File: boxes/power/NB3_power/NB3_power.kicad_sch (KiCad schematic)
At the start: 31 parts, among them J1 Barrel_Jack_PJ-036AH-SMT-TR, J2 Conn_01x04_Male, SW1 SW_SPDT, U1 Voltage_Regulator_AP64501

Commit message: Final draft (rev 0.0.1) of NB3_power PCB
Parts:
- added D2: LED, LED_SMD:LED_0603_1608Metric, symbol Device:LED
- added R6: 1.6k, Resistor_SMD:R_0402_1005Metric, symbol Device:R
- J2: footprint Connector_PinHeader_2.54mm:PinHeader_1x04_P2.54mm_Vertical_SMD_Pin1Right -> NB3_power:PinHeader_TSM-104-01-L-SH
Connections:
- net +5V: now also J2.1 (Pin_1), J2.2 (Pin_2), D2.2 (A); no longer J2.3 (Pin_3), J2.4 (Pin_4)
- net GND: now also J2.3 (Pin_3), J2.4 (Pin_4), R6.2; no longer J2.1 (Pin_1), J2.2 (Pin_2)
- new net: D2.1 (K), R6.1
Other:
- moved on the sheet: J2

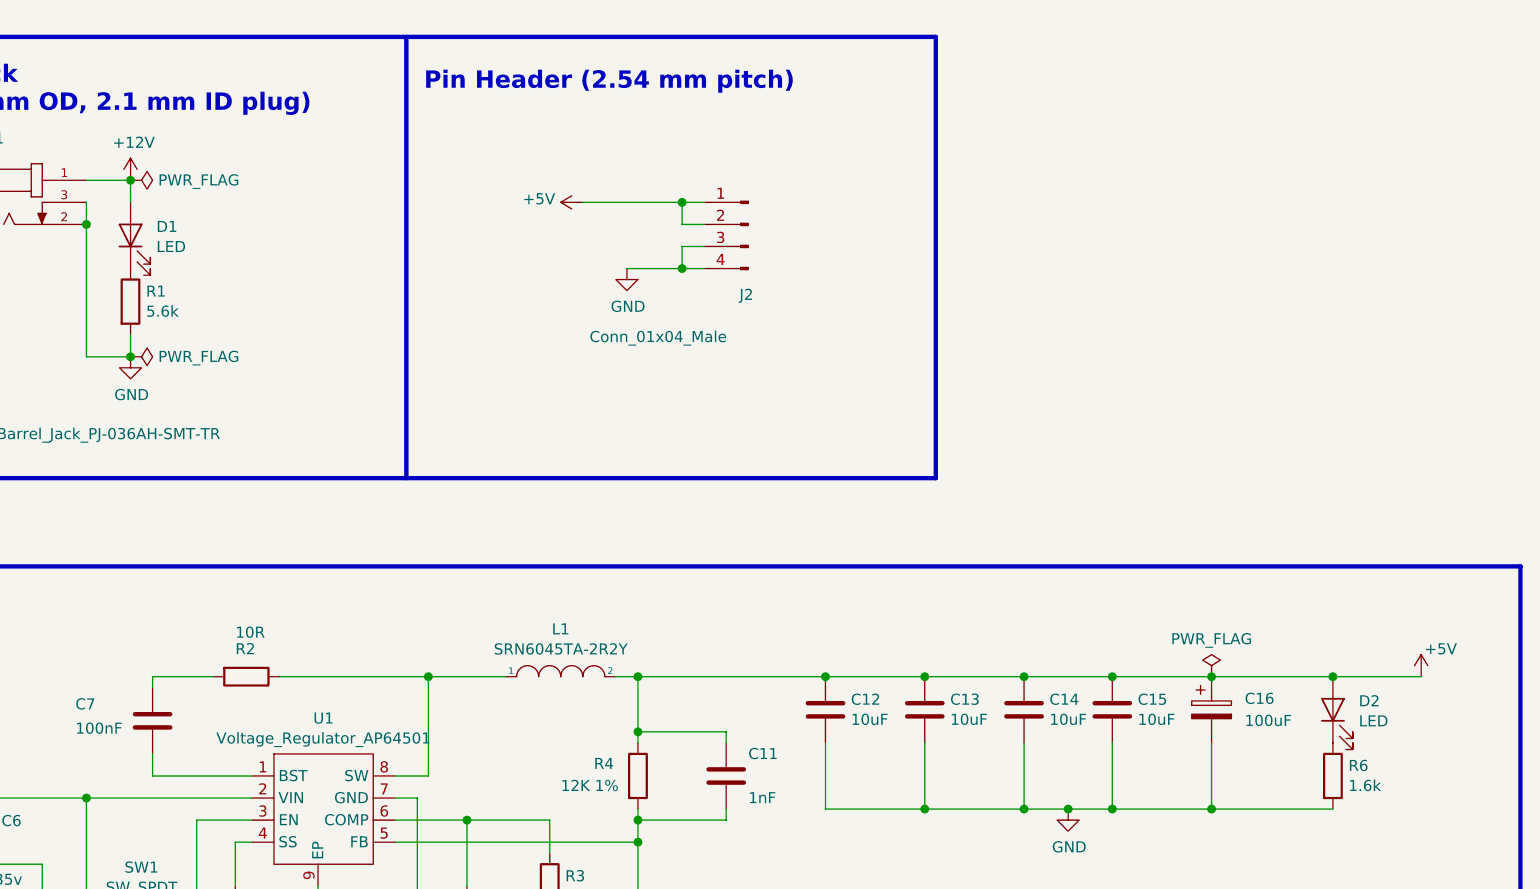
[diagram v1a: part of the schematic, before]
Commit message: Optimized NB3_power BOM for cost
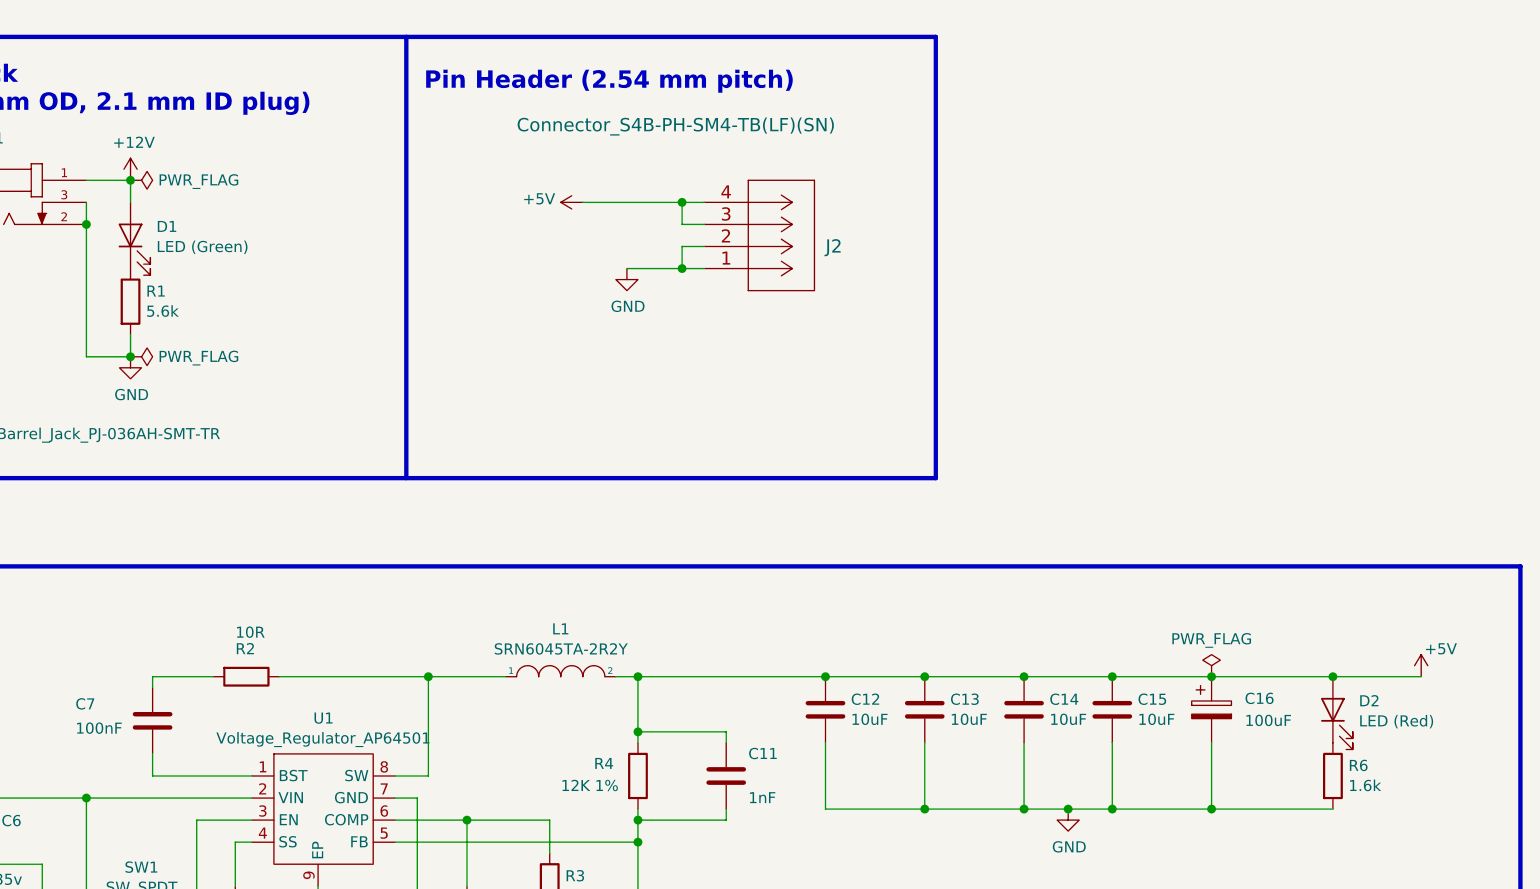
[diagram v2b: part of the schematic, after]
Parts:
- removed J2: Conn_01x04_Male, NB3_power:PinHeader_TSM-104-01-L-SH, symbol Connector:Conn_01x04_Male
- added J2: Connector_S4B-PH-SM4-TB(LF)(SN), NB3_power:Connector_S4B-PH-SM4-TB(LF)(SN), symbol NB3_power:Connector_S4B-PH-SM4-TB(LF)(SN)
- D1: value LED -> LED (Green)
- D2: value LED -> LED (Red)
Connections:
- net +5V: now also J2.3, J2.4
- net GND: now also J2.1, J2.2
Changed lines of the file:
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@@
       (effects (font (size 1.27 1.27)) (justify right))
     )
-    (property "Value" "LED" (id 1) (at 126.1618 54.6608 90)
+    (property "Value" "LED (Green)" (id 1) (at 126.1618 54.6608 90)
       (effects (font (size 1.27 1.27)) (justify right))
     )
@@
       (effects (font (size 1.27 1.27)) (justify right))
     )
-    (property "Value" "LED" (id 1) (at 264.5918 109.2708 90)
+    (property "Value" "LED (Red)" (id 1) (at 264.5918 109.2708 90)
       (effects (font (size 1.27 1.27)) (justify right))
     )
@@
     (pin "1")
     (pin "2")
-  )
-  (symbol (lib_id "Connector:Conn_01x04_Male") (at 194.31 52.07 0) (mirror y) (unit 1)
-    (in_bom yes) (on_board yes)
-    (property "Reference" "J2" (id 0) (at 194.1068 60.1726 0))
-    (property "Value" "Conn_01x04_Male" (id 1) (at 183.9468 65.024 0))
-    (property "Footprint" "NB3_power:PinHeader_TSM-104-01-L-SH" (id 2) (at 194.31 52.07 0)
-      (effects (font (size 1.27 1.27)) hide)
-    )
-    (property "Datasheet" "~" (id 3) (at 194.31 52.07 0)
-      (effects (font (size 1.27 1.27)) hide)
-    )
-    (pin "1")
-    (pin "2")
-    (pin "3")
-    (pin "4")
   )
   (symbol (lib_id "Switch:SW_SPDT") (at 124.46 133.35 0) (mirror y) (unit 1)
@@
     (pin "2")
     (pin "3")
+  )
+  (symbol (lib_id "NB3_power:Connector_S4B-PH-SM4-TB(LF)(SN)") (at 189.23 57.15 0) (mirror x) (unit 1)
+    (in_bom yes) (on_board yes)
+    (property "Reference" "J2" (id 0) (at 203.2 54.61 0)
+      (effects (font (size 1.524 1.524)) (justify left))
+    )
+    (property "Value" "Connector_S4B-PH-SM4-TB(LF)(SN)" (id 1) (at 167.64 40.64 0)
+      (effects (font (size 1.524 1.524)) (justify left))
+    )
+    (property "Footprint" "NB3_power:Connector_S4B-PH-SM4-TB(LF)(SN)" (id 2) (at 198.12 45.72 0)
+      (effects (font (size 1.524 1.524)) hide)
+    )
+    (property "Datasheet" "" (id 3) (at 189.23 57.15 0)
+      (effects (font (size 1.524 1.524)))
+    )
+    (pin "1")
+    (pin "2")
+    (pin "3")
+    (pin "4")
   )
   (symbol (lib_id "NB3_power:Logo_NBB") (at 49.53 72.39 0) (unit 1)
@@
     )
     (path "/00000000-0000-0000-0000-00005f87459f"
-      (reference "D1") (unit 1) (value "LED") (footprint "LED_SMD:LED_0603_1608Metric")
+      (reference "D1") (unit 1) (value "LED (Green)") (footprint "LED_SMD:LED_0603_1608Metric")
     )
     (path "/4e3ca639-512d-4aa0-b4b6-e1f8238c28ec"
-      (reference "D2") (unit 1) (value "LED") (footprint "LED_SMD:LED_0603_1608Metric")
+      (reference "D2") (unit 1) (value "LED (Red)") (footprint "LED_SMD:LED_0603_1608Metric")
     )
     (path "/39250da4-c637-43ee-a483-1f32947514fb"
@@
       (reference "J1") (unit 1) (value "Barrel_Jack_PJ-036AH-SMT-TR") (footprint "NB3_power:Barrel_Jack_PJ-036AH-SMT-TR")
     )
-    (path "/00000000-0000-0000-0000-00005f7c6cde"
-      (reference "J2") (unit 1) (value "Conn_01x04_Male") (footprint "NB3_power:PinHeader_TSM-104-01-L-SH")
+    (path "/ddf5b3ab-5704-4e10-8e98-e6581c198b1e"
+      (reference "J2") (unit 1) (value "Connector_S4B-PH-SM4-TB(LF)(SN)") (footprint "NB3_power:Connector_S4B-PH-SM4-TB(LF)(SN)")
     )
     (path "/32147c9a-74a8-45c4-9424-358946dc4fbc"

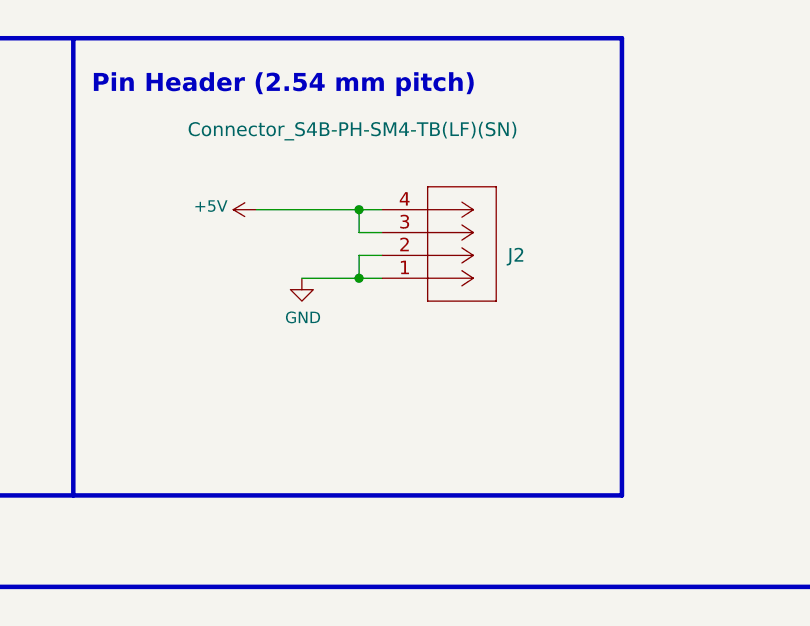
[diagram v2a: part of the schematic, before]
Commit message: NB3 pcb design tweaks
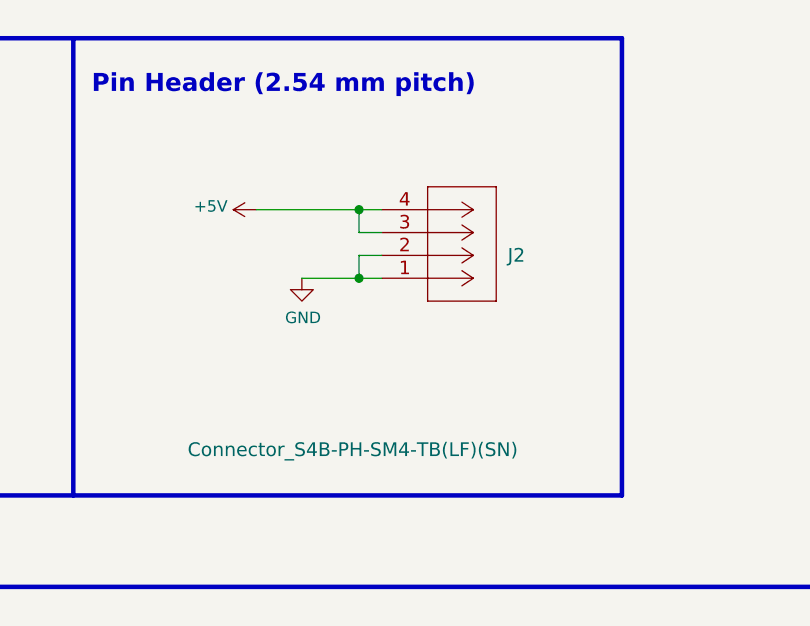
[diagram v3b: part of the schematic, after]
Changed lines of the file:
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@@
   (title_block
     (title "NB3 Power Board")
-    (date "2021-06-25")
-    (rev "0.0.1")
+    (date "2021-07-02")
+    (rev "0.0.2")
     (company "Voight-Kampff")
     (comment 1 "NoBlackBoxes: NB3 power source")
@@
       (effects (font (size 1.524 1.524)) (justify left))
     )
-    (property "Value" "Connector_S4B-PH-SM4-TB(LF)(SN)" (id 1) (at 167.64 40.64 0)
+    (property "Value" "Connector_S4B-PH-SM4-TB(LF)(SN)" (id 1) (at 167.64 76.2 0)
       (effects (font (size 1.524 1.524)) (justify left))
     )

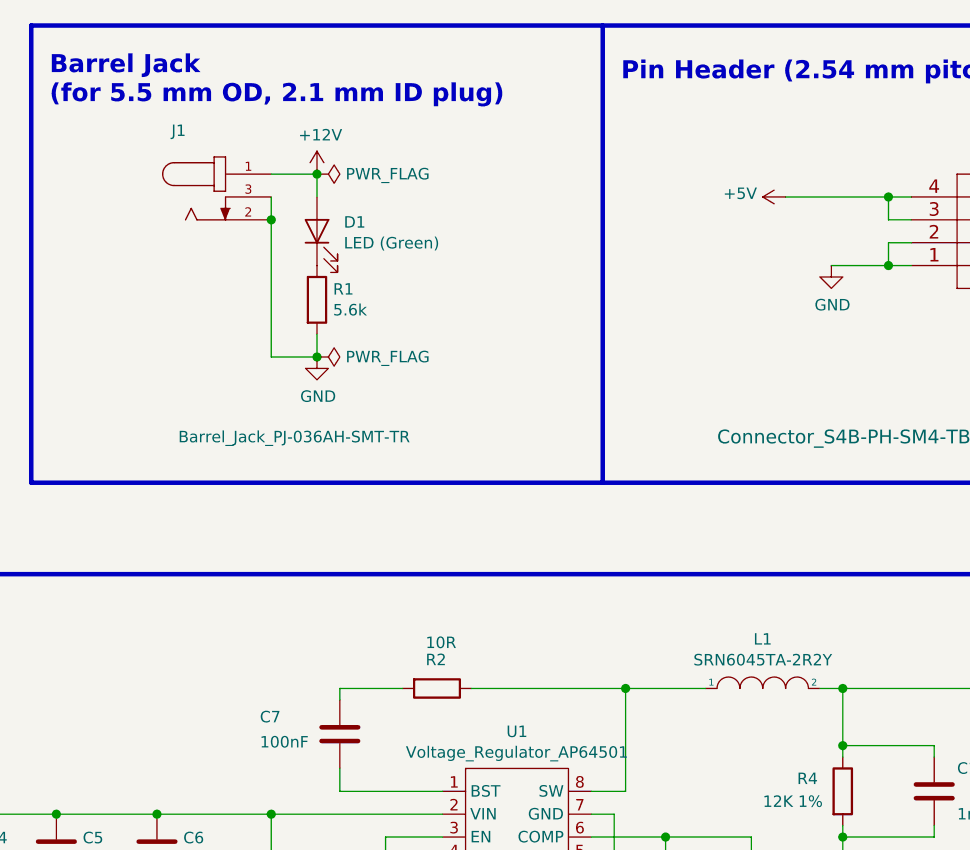
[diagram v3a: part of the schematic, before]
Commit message: Updated NB3_power: compatible w/replacement PS
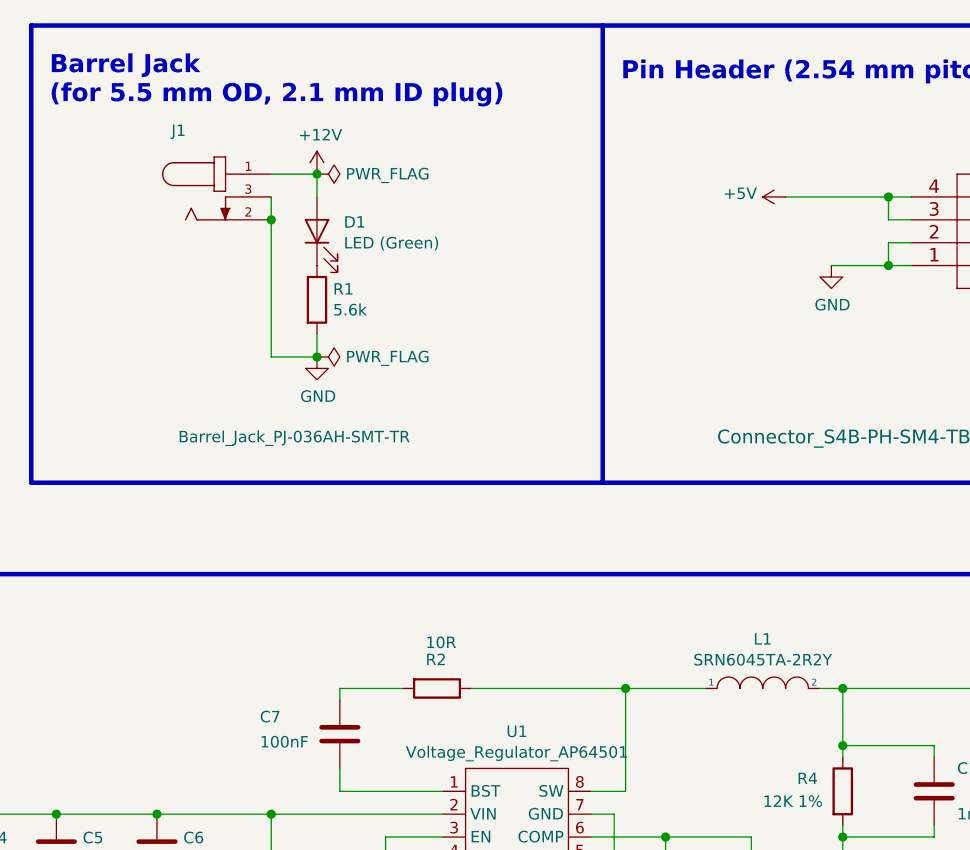
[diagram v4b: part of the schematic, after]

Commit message: Update NB3_power (R&E Only)
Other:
- moved on the sheet: C6, J1

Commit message: Update NB£_power (v4)
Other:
- note added: "For Research and Education ONLY"
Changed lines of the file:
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@@
     (effects (font (size 2 2) (thickness 0.4) bold) (justify right bottom))
+  )
+  (text "For Research and Education ONLY" (at 13.97 196.85 0)
+    (effects (font (size 2.54 2.54)) (justify left bottom))
   )
   (text "Barrel Jack\n(for 5.5 mm OD, 2.1 mm ID plug)" (at 93.472 39.37 0)
